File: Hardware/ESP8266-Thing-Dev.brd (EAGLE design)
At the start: 55.2 x 25.7 mm, 69 parts, among them J1 DNP, Q1 MMBT2222A, Q2 MMBT2222A, U1 AP2112K-3.3V, U2 ESP8266, U3 AT25SF041-SOIC8, U4 FTS31XS-U, Y1 26MHz

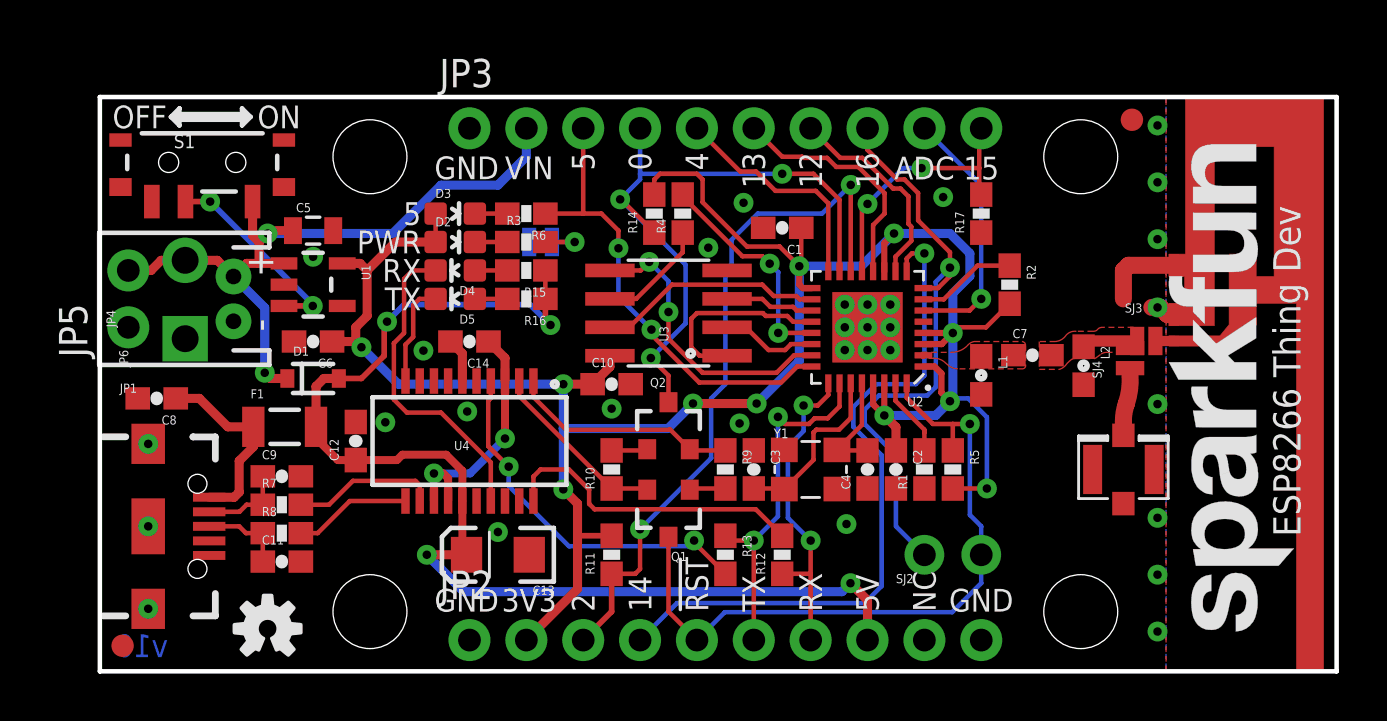
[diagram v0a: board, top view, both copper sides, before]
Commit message: Bumping out dimensions to a 0.01in grid.
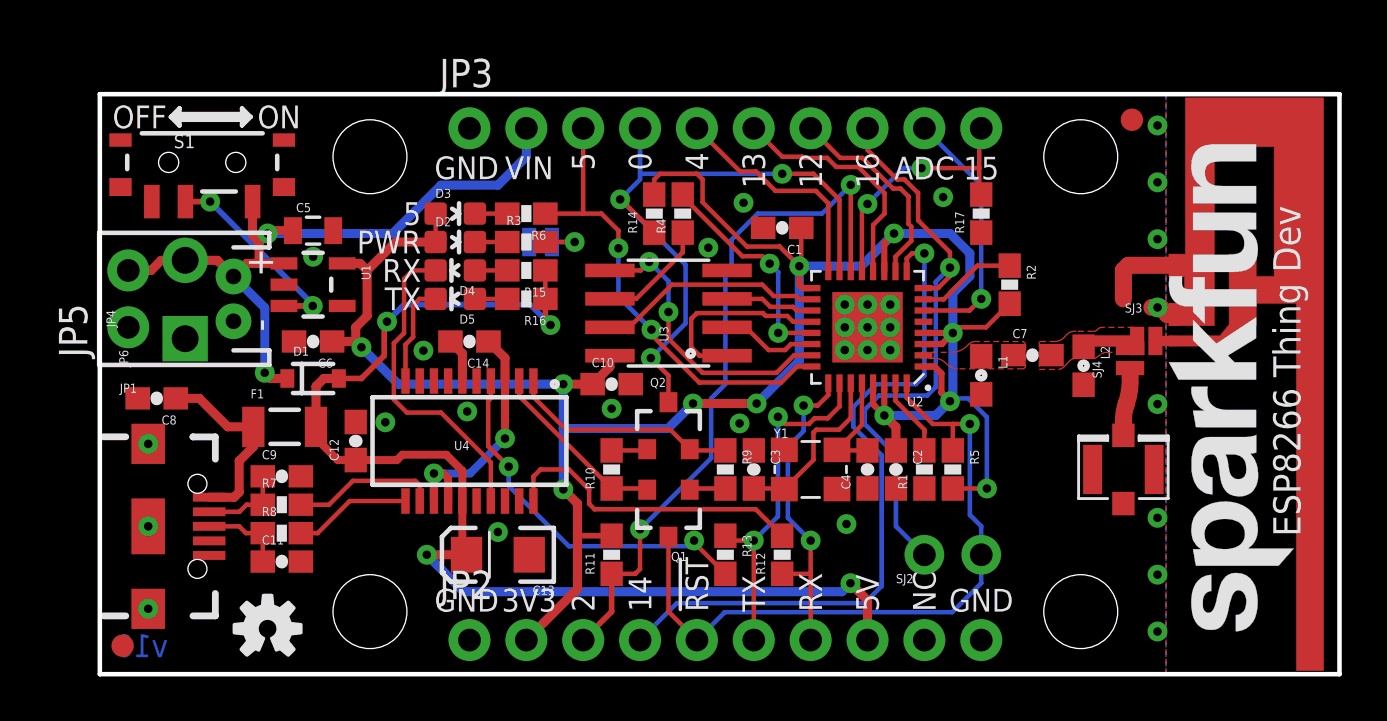
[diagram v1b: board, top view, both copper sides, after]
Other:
- board size 55.2 x 25.7 mm -> 55.4 x 25.9 mm
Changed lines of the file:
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@@
 <setting verticaltext="up"/>
 </settings>
-<grid distance="0.05" unitdist="inch" unit="inch" style="lines" multiple="1" display="yes" altdistance="0.0025" altunitdist="inch" altunit="inch"/>
+<grid distance="0.05" unitdist="inch" unit="inch" style="lines" multiple="1" display="yes" altdistance="0.005" altunitdist="inch" altunit="inch"/>
 <layers>
 <layer number="1" name="Top" color="4" fill="1" visible="yes" active="yes"/>
@@
 <board>
 <plain>
-<wire x1="0" y1="-0.127" x2="0" y2="25.527" width="0.2032" layer="20"/>
-<wire x1="0" y1="25.527" x2="55.245" y2="25.527" width="0.2032" layer="20"/>
-<wire x1="55.245" y1="25.527" x2="55.245" y2="-0.127" width="0.2032" layer="20"/>
-<wire x1="55.245" y1="-0.127" x2="0" y2="-0.127" width="0.2032" layer="20"/>
+<wire x1="0" y1="-0.254" x2="0" y2="25.654" width="0.2032" layer="20"/>
+<wire x1="0" y1="25.654" x2="55.372" y2="25.654" width="0.2032" layer="20"/>
+<wire x1="55.372" y1="25.654" x2="55.372" y2="-0.254" width="0.2032" layer="20"/>
+<wire x1="55.372" y1="-0.254" x2="0" y2="-0.254" width="0.2032" layer="20"/>
 <text x="1.778" y="24.638" size="1.016" layer="21" font="vector" ratio="15" align="center">OFF</text>
 <text x="8.001" y="24.638" size="1.016" layer="21" font="vector" ratio="15" align="center">ON</text>
@@
 <text x="3.048" y="1.016" size="1.016" layer="16" font="vector" ratio="15" rot="MR0" align="center-left">v10</text>
 <text x="19.685" y="17.78" size="1.016" layer="22" font="vector" ratio="15" rot="MR0" align="top-center">PWR-LED</text>
-<dimension x1="0" y1="-0.127" x2="55.245" y2="0" x3="27.6225" y3="-11.43" textsize="1.016" textratio="15" layer="47" dtype="horizontal" unit="inch" precision="3"/>
-<dimension x1="0" y1="-0.127" x2="43.815" y2="2.54" x3="21.9075" y3="-8.89" textsize="1.016" textratio="15" layer="47" dtype="horizontal" unit="inch" precision="3"/>
-<dimension x1="0" y1="-0.127" x2="12.065" y2="2.54" x3="6.0325" y3="-3.81" textsize="1.016" textratio="15" layer="47" dtype="horizontal" unit="inch" precision="3"/>
-<dimension x1="0" y1="-0.127" x2="16.51" y2="1.27" x3="8.255" y3="-6.35" textsize="1.016" textratio="15" layer="47" dtype="horizontal" unit="inch" precision="3"/>
-<dimension x1="0" y1="-0.127" x2="0" y2="25.527" x3="-11.43" y3="12.7" textsize="1.016" textratio="15" layer="47" dtype="vertical" unit="inch" precision="3"/>
-<dimension x1="0" y1="-0.127" x2="12.065" y2="2.54" x3="-3.81" y3="1.2065" textsize="1.016" textratio="15" layer="47" dtype="vertical" unit="inch" precision="3"/>
-<dimension x1="0" y1="-0.127" x2="16.51" y2="1.27" x3="-1.27" y3="0.5715" textsize="1.016" textratio="15" layer="47" dtype="vertical" unit="inch" precision="3"/>
-<dimension x1="0" y1="-0.127" x2="16.51" y2="24.13" x3="-8.89" y3="12.0015" textsize="1.016" textratio="15" layer="47" dtype="vertical" unit="inch" precision="3"/>
-<dimension x1="0" y1="-0.127" x2="12.065" y2="22.86" x3="-6.35" y3="11.3665" textsize="1.016" textratio="15" layer="47" dtype="vertical" unit="inch" precision="3"/>
+<dimension x1="0" y1="-0.254" x2="55.372" y2="0" x3="27.686" y3="-11.43" textsize="1.016" textratio="15" layer="47" dtype="horizontal" unit="inch" precision="3"/>
+<dimension x1="0" y1="-0.254" x2="43.815" y2="2.54" x3="21.9075" y3="-8.89" textsize="1.016" textratio="15" layer="47" dtype="horizontal" unit="inch" precision="3"/>
+<dimension x1="0" y1="-0.254" x2="12.065" y2="2.54" x3="6.0325" y3="-3.81" textsize="1.016" textratio="15" layer="47" dtype="horizontal" unit="inch" precision="3"/>
+<dimension x1="0" y1="-0.254" x2="16.51" y2="1.27" x3="8.255" y3="-6.35" textsize="1.016" textratio="15" layer="47" dtype="horizontal" unit="inch" precision="3"/>
+<dimension x1="0" y1="-0.254" x2="0" y2="25.654" x3="-11.43" y3="12.7" textsize="1.016" textratio="15" layer="47" dtype="vertical" unit="inch" precision="3"/>
+<dimension x1="0" y1="-0.254" x2="12.065" y2="2.54" x3="-3.81" y3="1.143" textsize="1.016" textratio="15" layer="47" dtype="vertical" unit="inch" precision="3"/>
+<dimension x1="0" y1="-0.254" x2="16.51" y2="1.27" x3="-1.27" y3="0.508" textsize="1.016" textratio="15" layer="47" dtype="vertical" unit="inch" precision="3"/>
+<dimension x1="0" y1="-0.254" x2="16.51" y2="24.13" x3="-8.89" y3="11.938" textsize="1.016" textratio="15" layer="47" dtype="vertical" unit="inch" precision="3"/>
+<dimension x1="0" y1="-0.254" x2="12.065" y2="22.86" x3="-6.35" y3="11.303" textsize="1.016" textratio="15" layer="47" dtype="vertical" unit="inch" precision="3"/>
 <text x="25.4" y="-21.59" size="1.27" layer="51" font="vector" ratio="15">Jim Lindblom</text>
 <text x="-17.78" y="-7.62" size="1.27" layer="47" font="vector" ratio="15">Units in Inches</text>
@@
 <contactref element="S1" pad="1"/>
 <polygon width="0.254" layer="16" isolate="0.3048" rank="6">
-<vertex x="0" y="-0.127"/>
-<vertex x="0" y="25.527"/>
-<vertex x="47.625" y="25.527"/>
-<vertex x="47.625" y="-0.127"/>
+<vertex x="0" y="-0.254"/>
+<vertex x="0" y="25.654"/>
+<vertex x="47.625" y="25.654"/>
+<vertex x="47.625" y="-0.254"/>
 </polygon>
 <polygon width="0.254" layer="1" isolate="0.3048" rank="6">
-<vertex x="0" y="25.527"/>
-<vertex x="0" y="-0.127"/>
-<vertex x="47.625" y="-0.127"/>
-<vertex x="47.625" y="25.527"/>
+<vertex x="0" y="25.654"/>
+<vertex x="0" y="-0.254"/>
+<vertex x="47.625" y="-0.254"/>
+<vertex x="47.625" y="25.654"/>
 </polygon>
 <via x="34.29" y="15.24" extent="1-16" drill="0.381"/>

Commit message: moved fiducials inward for better recognition
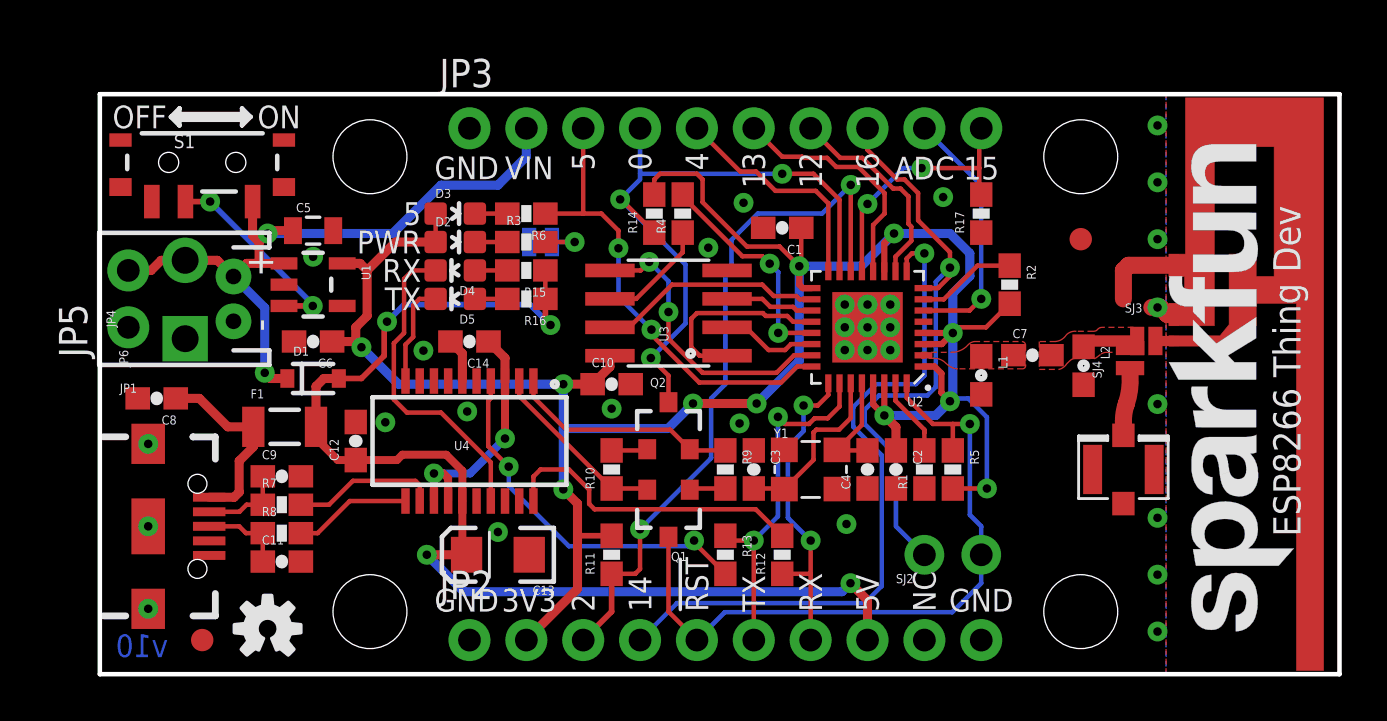
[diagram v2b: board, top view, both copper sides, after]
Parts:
- moved FID1 5.80 mm to (43.8, 19.2)
- moved FID2 3.57 mm to (4.57, 1.27)
